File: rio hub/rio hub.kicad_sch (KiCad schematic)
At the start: 1 part

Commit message: fixed diode placement, major rio hub work
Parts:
- removed U1: ~, FRC:RoboRIO-THT, symbol FRC:RoboRIO
- added D1: D_Schottky, Diode_THT:D_DO-41_SOD81_P10.16mm_Horizontal, symbol Device:D_Schottky
- added J1, J3: Conn_01x02_Pin, Connector_PinHeader_2.54mm:PinHeader_1x02_P2.54mm_Vertical, symbol Connector:Conn_01x02_Pin
- added J2: Conn_01x02_Pin, TerminalBlock_WAGO:TerminalBlock_WAGO_2601-1102_1x02_P3.50mm_Horizontal, symbol Connector:Conn_01x02_Pin
- added J4: MTJ-88ARX1-FSM-LG, custom:ADAMTECH_MTJ-88ARX1-FSM-LG, symbol MTJ-88ARX1-FSM-LG:MTJ-88ARX1-FSM-LG
- added J5: Conn_02x17_Odd_Even, symbol Connector_Generic:Conn_02x17_Odd_Even
- added J6: Conn_01x04_Socket, symbol Connector:Conn_01x04_Socket
- added R1: R, Resistor_THT:R_Axial_DIN0207_L6.3mm_D2.5mm_P10.16mm_Horizontal, symbol Device:R
- added U1: ~, FRC:RoboRIO_MXP-THT, symbol FRC:RoboRIO-MXP-Port_Conn_02x17
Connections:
- new net: D1.2 (A), J2.1 (Pin_1)
- new net: J5.1 (Pin_1), U1.1 (MXP_5V)
- new net: J5.10 (Pin_10), U1.10 (MXP_RX)
- new net: J5.11 (Pin_11), U1.11 (MXP_DIO0_PWM0)
- new net: J5.13 (Pin_13), U1.13 (MXP_DIO1_PWM1)
- new net: J5.14 (Pin_14), U1.14 (MXP_TX)
- new net: J5.15 (Pin_15), U1.15 (MXP_DIO2_PWM2)
- new net: J5.17 (Pin_17), U1.17 (MXP_DIO3_PWM3)
- new net: J5.18 (Pin_18), U1.18 (MXP_DIO11_PWM7)
- new net: J5.19 (Pin_19), U1.19 (MXP_DIO4_CS)
- new net: J5.2 (Pin_2), U1.2 (MXP_AO0)
- new net: J5.21 (Pin_21), U1.21 (MXP_DIO5_SCLK)
- new net: J5.22 (Pin_22), U1.22 (MXP_DIO12_PWM8)
- new net: J5.23 (Pin_23), U1.23 (MXP_DIO6_MISO)
- new net: J5.25 (Pin_25), U1.25 (MXP_DIO7_MOSI)
- new net: J5.26 (Pin_26), U1.26 (MXP_DIO13_PWM9)
- new net: J5.27 (Pin_27), U1.27 (MXP_DIO8_PWM4)
- new net: J5.29 (Pin_29), U1.29 (MXP_DIO9_PWM5)
- new net: J5.3 (Pin_3), U1.3 (MXP_AI0)
- new net: J5.31 (Pin_31), U1.31 (MXP_DIO10_PWM6)
- new net: J5.32 (Pin_32), U1.32 (MXP_DIO14_SCL)
- new net: J5.33 (Pin_33), U1.33 (MXP_3V3)
- new net: J5.34 (Pin_34), U1.34 (MXP_DIO15_SDA)
- new net: J5.4 (Pin_4), U1.4 (MXP_AO1)
- new net: J5.5 (Pin_5), U1.5 (MXP_AI1)
- new net: J5.7 (Pin_7), U1.7 (MXP_AI2)
- new net: J5.9 (Pin_9), U1.9 (MXP_AI3)
- new net: J4.9, R1.1
- new net: J1.1 (Pin_1), J4.1
- new net: J1.2 (Pin_2), J4.2
- new net: J4.5, J6.1 (Pin_1)
- new net: J4.6, J6.2 (Pin_2)
- new net: J4.7, J6.3 (Pin_3)
- new net: J4.8, J6.4 (Pin_4)
- new net 12v: D1.1 (K), J3.1 (Pin_1), J4.10, J4.3
- new net AGND: J5.6 (Pin_6), U1.6 (MXP_AGND)
- new net DGND: J5.12 (Pin_12), J5.16 (Pin_16), J5.20 (Pin_20), J5.24 (Pin_24), J5.28 (Pin_28), J5.30 (Pin_30), J5.8 (Pin_8), U1.12 (MXP_DGND), U1.16 (MXP_DGND), U1.20 (MXP_DGND), U1.24 (MXP_DGND), U1.28 (MXP_DGND), U1.30 (MXP_DGND), U1.8 (MXP_DGND)
- new net GND: J2.2 (Pin_2), J3.2 (Pin_2), J4.4, J4.SH1 (SHIELD), J4.SH2 (SHIELD__1), R1.2
- no-connect marks 0 -> 2

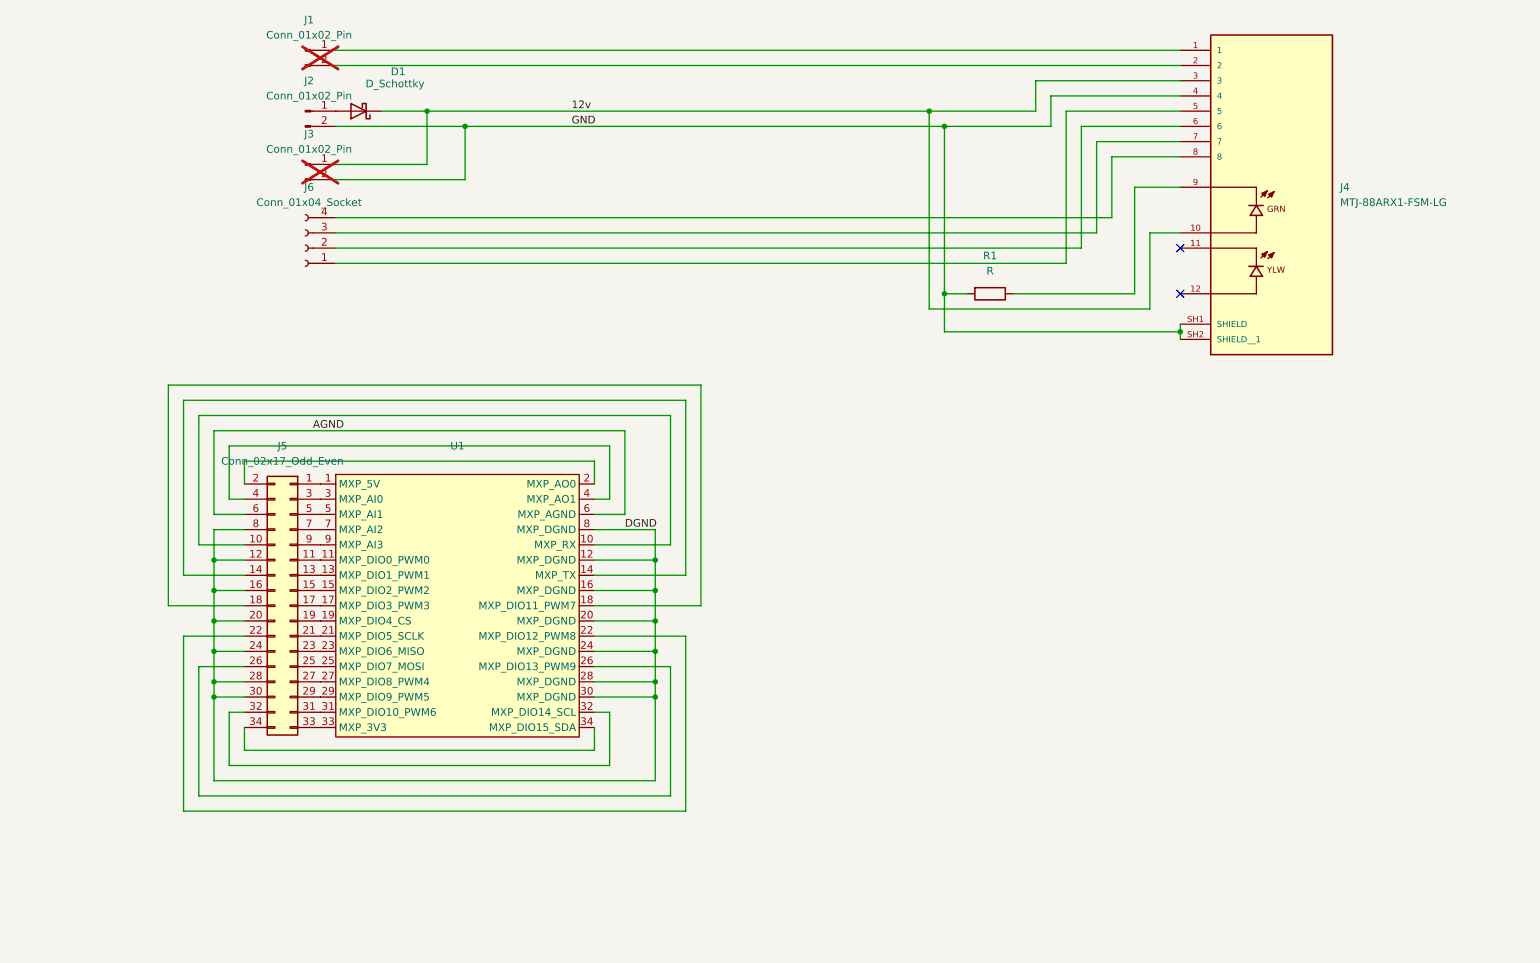
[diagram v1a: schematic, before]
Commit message: removed mxp crossover, moved to hardwired DIO, switching from DIO WAGOs to Molex SL
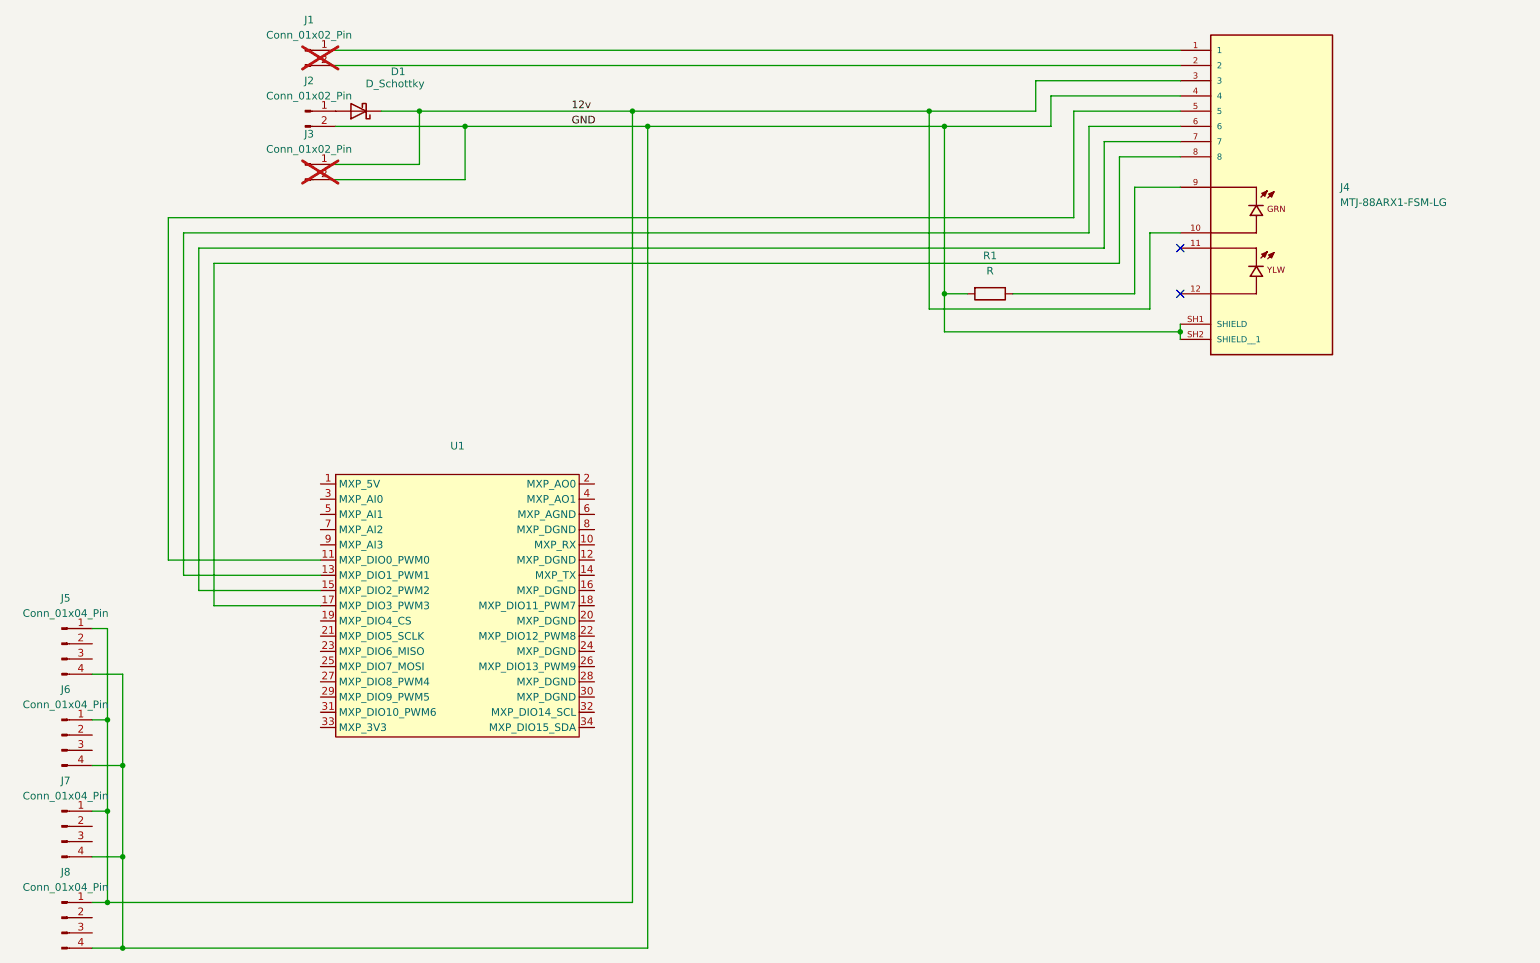
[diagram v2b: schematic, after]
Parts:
- removed J5: Conn_02x17_Odd_Even, symbol Connector_Generic:Conn_02x17_Odd_Even
- removed J6: Conn_01x04_Socket, symbol Connector:Conn_01x04_Socket
- added J5, J6, J7, J8: Conn_01x04_Pin, symbol Connector:Conn_01x04_Pin
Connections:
- net 12v: now also J5.1 (Pin_1), J6.1 (Pin_1), J7.1 (Pin_1), J8.1 (Pin_1)
- net GND: now also J5.4 (Pin_4), J6.4 (Pin_4), J7.4 (Pin_4), J8.4 (Pin_4)
- net at U1.11 (MXP_DIO0_PWM0): now also J4.5
- net at U1.13 (MXP_DIO1_PWM1): now also J4.6
- net at U1.15 (MXP_DIO2_PWM2): now also J4.7
- net at U1.17 (MXP_DIO3_PWM3): now also J4.8
- net AGND: no longer names the net of U1.6 (MXP_AGND)
- removed net DGND: U1.12 (MXP_DGND), U1.16 (MXP_DGND), U1.20 (MXP_DGND), U1.24 (MXP_DGND), U1.28 (MXP_DGND), U1.30 (MXP_DGND), U1.8 (MXP_DGND)

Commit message: added features claimed to be from previous commit
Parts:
- added J10, J9: Conn_01x03_Pin, custom:Molex_SL_171971-0003_1x03_P2.54mm_Vertical, symbol Connector:Conn_01x03_Pin
- J5, J6, J7, J8: footprint (none) -> custom:Molex_SL_171971-0004_1x04_P2.54mm_Vertical
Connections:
- net GND: now also U1.12 (MXP_DGND), U1.16 (MXP_DGND), U1.20 (MXP_DGND), U1.24 (MXP_DGND), U1.28 (MXP_DGND), U1.30 (MXP_DGND), U1.6 (MXP_AGND), U1.8 (MXP_DGND), J10.3 (Pin_3), J9.3 (Pin_3)
- net at J7.2 (Pin_2): now also U1.27 (MXP_DIO8_PWM4)
- net at J7.3 (Pin_3): now also U1.29 (MXP_DIO9_PWM5)
- net at J6.2 (Pin_2): now also U1.23 (MXP_DIO6_MISO)
- net at J6.3 (Pin_3): now also U1.25 (MXP_DIO7_MOSI)
- net at U1.1 (MXP_5V): now also J10.2 (Pin_2), J9.2 (Pin_2)
- net at U1.18 (MXP_DIO11_PWM7): now also J10.1 (Pin_1)
- net at U1.19 (MXP_DIO4_CS): now also J5.2 (Pin_2)
- net at U1.21 (MXP_DIO5_SCLK): now also J5.3 (Pin_3)
- net at U1.22 (MXP_DIO12_PWM8): now also J8.2 (Pin_2)
- net at U1.26 (MXP_DIO13_PWM9): now also J8.3 (Pin_3)
- net at U1.31 (MXP_DIO10_PWM6): now also J9.1 (Pin_1)
